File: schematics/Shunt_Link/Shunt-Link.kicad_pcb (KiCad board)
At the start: 2 copper layers, 20.3 x 8.4 mm, 17 parts, among them IC1 AD8221TRMZ-EP, IC2 AD8221TRMZ-EP, IC3 AD8244ARMZ, J1 PCIe_1x_Bus, J2 Conn_01x05_Socket

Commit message: Updated to git
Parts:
- removed IC3: AD8244ARMZ, APT_Needs:AD8244ARMZ
- added L1: AD8244ARMZ, Link_Footprints:AD8244ARMZ, F.Cu at (98.7, 79.2)
- D1: value LED_Lights -> WP130WCP_2EGW; footprint APT_Needs:LED_Lights -> Link_Footprints:LED_Lights
- IC1, IC2: footprint APT_Needs:AD8221TRMZ-EP -> Link_Footprints:AD8221TRMZ-EP
- J1: value PCIe_1x_Bus -> PCIE-036-02-X-D-TH; footprint Connector_PCBEdge:BUS_PCIexpress_x1 -> Link_Footprints:SAMTEC_PCIE_1x
- J2: footprint APT_Needs:Phoenix_Contact_MSTBA-LR -> Link_Footprints:Phoenix_Contact_MSTBA,5-LR
- TP1, TP2, TP3: value Keystone_1045 -> 1045; footprint APT_Needs:Keystone_1045 -> Link_Footprints:Keystone_1045
- moved R5 60.3 mm to (92.8, 61.8)
- moved R6 60.3 mm to (92.8, 64.8)
- moved D1 46.7 mm to (100.0, 68.9)
- moved R1 41.2 mm to (92.8, 50.0)
- moved R2 41.2 mm to (92.8, 53.0)
- moved R3 41.2 mm to (92.8, 55.9)
- moved R4 41.2 mm to (92.8, 58.9)
- moved Rg_1 36.8 mm to (92.8, 67.7)
- moved Rg_2 36.8 mm to (92.8, 70.7)
- moved J1 33.9 mm to (117.5, 80.9)
- moved TP1 33.3 mm to (115.2, 65.6)
- moved TP2 33.3 mm to (115.2, 69.7)
- moved TP3 33.3 mm to (115.2, 73.8)
- moved J2 29.3 mm to (104.8, 52.1), turned to 0 degrees
- moved IC2 16.5 mm to (125.8, 70.7)
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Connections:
- J1 pad A1: unconnected-(J1-PadA1) -> /NC
- J1 pad A10: unconnected-(J1-PadA10) -> /NC
- J1 pad A11: unconnected-(J1-PadA11) -> /NC
- J1 pad A12: unconnected-(J1-PadA12) -> /NC
- J1 pad A13: unconnected-(J1-PadA13) -> /NC
- J1 pad A14: unconnected-(J1-PadA14) -> /NC
- J1 pad A15: unconnected-(J1-PadA15) -> /NC
- J1 pad A16: unconnected-(J1-PadA16) -> /NC
- J1 pad A17: unconnected-(J1-PadA17) -> /NC
- J1 pad A18: unconnected-(J1-PadA18) -> /NC
- J1 pad A2: unconnected-(J1-PadA2) -> /NC
- J1 pad A3: unconnected-(J1-PadA3) -> /NC
- J1 pad A4: unconnected-(J1-PadA4) -> /NC
- J1 pad A5: unconnected-(J1-PadA5) -> /NC
- J1 pad A6: unconnected-(J1-PadA6) -> /NC
- J1 pad A7: unconnected-(J1-PadA7) -> /NC
- J1 pad A8: unconnected-(J1-PadA8) -> /NC
- J1 pad A9: unconnected-(J1-PadA9) -> /NC
- J1 pad B14: unconnected-(J1-PadB14) -> /NC
- J1 pad B15: unconnected-(J1-PadB15) -> /NC
- J1 pad B16: unconnected-(J1-PadB16) -> /NC
- J1 pad B3: unconnected-(J1-PadB3) -> /NC
- J1 pad B4: unconnected-(J1-PadB4) -> /NC
- J1 pad B5: unconnected-(J1-PadB5) -> /NC
- J1 pad B6: unconnected-(J1-PadB6) -> /NC
- J1 pad B7: unconnected-(J1-PadB7) -> /NC
- J1 pad B8: unconnected-(J1-PadB8) -> /NC
- J1 pad B9: unconnected-(J1-PadB9) -> /NC
- TP1 pad TP1: /S_{o} -> /S_{test}
- TP2 pad TP1: /T_{o} -> /T_{test}
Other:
- board outline removed

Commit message: Modifications to Shunt Link
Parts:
- removed D1: WP130WCP_2EGW, Link_Footprints:LED_Lights
- removed Rg_1, Rg_2: 499, Resistor_SMD:R_0805_2012Metric
- added C1: 0.1 uF, Capacitor_SMD:C_1210_3225Metric, F.Cu at (138.8, 56.5)
- added C2: 10 uF, Capacitor_SMD:C_1210_3225Metric, F.Cu at (146.5, 56.5)
- added IC3: AD8221TRMZ-EP, Link_Footprints:AD8221TRMZ-EP, F.Cu at (135.5, 99.7)
- added IC4: AD8221TRMZ-EP, Link_Footprints:AD8221TRMZ-EP, F.Cu at (135.2, 110.0)
- added J3: Conn_02x03_Odd_Even, Link_Footprints:1818517, F.Cu at (90.8, 100.5)
- added R10: R, Resistor_SMD:R_2512_6332Metric, F.Cu at (111.8, 109.8)
- added R11: R, Resistor_SMD:R_2512_6332Metric, F.Cu at (117.2, 116.0)
- added R12: R, Resistor_SMD:R_2512_6332Metric, F.Cu at (121.2, 109.9)
- added R7: R_{g3}, Resistor_SMD:R_2512_6332Metric, F.Cu at (127.8, 99.7)
- added R8: R_{shunt}, Resistor_SMD:R_2512_6332Metric, F.Cu at (122.0, 99.7)
- added R9: R_{g4}, Resistor_SMD:R_2512_6332Metric, F.Cu at (127.5, 110.0)
- added TP4: T2, Link_Footprints:KEYSTONE_5017, F.Cu at (111.5, 39.8)
- added TP5: GND, Link_Footprints:KEYSTONE_5017, F.Cu at (90.2, 50.2)
- J1: footprint Link_Footprints:SAMTEC_PCIE_1x -> Connector_PCBEdge:BUS_PCIexpress_x1
- J2: value Conn_01x05_Socket -> Conn_02x03_Odd_Even; footprint Link_Footprints:Phoenix_Contact_MSTBA,5-LR -> Link_Footprints:1818517
- R1: value 6.25 -> R_{g1}; footprint Resistor_SMD:R_0805_2012Metric -> Resistor_SMD:R_2512_6332Metric
- R2: value 6.25 -> R_{shunt}; footprint Resistor_SMD:R_0805_2012Metric -> Resistor_SMD:R_2512_6332Metric
- R3: value 10.4 -> R_{g2}; footprint Resistor_SMD:R_0805_2012Metric -> Resistor_SMD:R_2512_6332Metric
- R4, R5: value 50 -> R; footprint Resistor_SMD:R_0805_2012Metric -> Resistor_SMD:R_2512_6332Metric
- R6: value 20.8 -> R; footprint Resistor_SMD:R_0805_2012Metric -> Resistor_SMD:R_2512_6332Metric
- TP1: value 1045 -> S1; footprint Link_Footprints:Keystone_1045 -> Link_Footprints:KEYSTONE_5017
- TP2: value 1045 -> T1; footprint Link_Footprints:Keystone_1045 -> Link_Footprints:KEYSTONE_5017
- TP3: value 1045 -> S2; footprint Link_Footprints:Keystone_1045 -> Link_Footprints:KEYSTONE_5017
- moved J1 50.4 mm to (136.0, 127.8)
- moved L1 43.1 mm to (102.0, 36.2)
- moved TP3 42.5 mm to (90.2, 39.4)
- moved R3 41.4 mm to (128.0, 77.7), turned to -90 degrees
- moved TP1 41.3 mm to (90.2, 32.8)
- moved TP2 37.1 mm to (111.5, 32.8)
- moved R1 35.9 mm to (124.8, 66.2), turned to -90 degrees
- moved R5 33.9 mm to (118.2, 84.2), turned to 180 degrees
- moved R6 31.3 mm to (121.2, 77.7), turned to -90 degrees
- moved R4 28.7 mm to (114.5, 77.6), turned to -90 degrees
- moved R2 27.6 mm to (117.0, 66.2), turned to -90 degrees
- moved J2 20.3 mm to (91.0, 67.0), turned to -90 degrees
- moved IC2 11.8 mm to (135.2, 77.8)
- moved IC1 9.24 mm to (135.0, 66.0)
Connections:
- IC1 pad 1: /S_{+} -> /S_{1+}
- IC1 pad 4: /GND -> GND
- IC1 pad 5: /GND -> GND
- IC1 pad 6: /V_{ref} -> /+2V5
- IC1 pad 7: /S_{o} -> /S_{1out}
- IC1 pad 8: /V_{s} -> +12V
- IC2 pad 1: /T_{+} -> /T_{1-}
- IC2 pad 4: /GND -> Net-(IC2-+IN)
- IC2 pad 5: /GND -> GND
- IC2 pad 7: /T_{o} -> /T_{1out}
- IC2 pad 8: /V_{s} -> unconnected-(IC2-+VS-Pad8)
- J1 pad A1: /NC -> unconnected-(J1-PadA1)
- J1 pad A10: /NC -> unconnected-(J1-PadA10)
- J1 pad A11: /NC -> unconnected-(J1-PadA11)
- J1 pad A12: /NC -> unconnected-(J1-PadA12)
- J1 pad A13: /NC -> unconnected-(J1-PadA13)
- J1 pad A14: /NC -> unconnected-(J1-PadA14)
- J1 pad A15: /NC -> unconnected-(J1-PadA15)
- J1 pad A16: /NC -> unconnected-(J1-PadA16)
- J1 pad A17: /NC -> unconnected-(J1-PadA17)
- J1 pad A18: /NC -> unconnected-(J1-PadA18)
- J1 pad A2: /NC -> unconnected-(J1-PadA2)
- J1 pad A3: /NC -> unconnected-(J1-PadA3)
- J1 pad A4: /NC -> unconnected-(J1-PadA4)
- J1 pad A5: /NC -> unconnected-(J1-PadA5)
- J1 pad A6: /NC -> unconnected-(J1-PadA6)
- J1 pad A7: /NC -> unconnected-(J1-PadA7)
- J1 pad A8: /NC -> unconnected-(J1-PadA8)
- J1 pad A9: /NC -> unconnected-(J1-PadA9)
- J1 pad B1: /S_{o} -> /S_{2out}
- J1 pad B10: /Green_{1} -> unconnected-(J1-PadB10)
- J1 pad B11: /Red_{1} -> unconnected-(J1-PadB11)
- J1 pad B12: /Green_{2} -> unconnected-(J1-PadB12)
- J1 pad B13: /Red_{2} -> unconnected-(J1-PadB13)
- J1 pad B14: /NC -> unconnected-(J1-PadB14)
- J1 pad B15: /NC -> unconnected-(J1-PadB15)
- J1 pad B16: /NC -> unconnected-(J1-PadB16)
- J1 pad B17: /V_{s} -> +12V
- J1 pad B18: /GND -> GND
- J1 pad B2: /T_{o} -> /T_{2out}
- J1 pad B3: /NC -> /T_{1out}
- J1 pad B4: /NC -> /S_{1out}
- J1 pad B5: /NC -> unconnected-(J1-PadB5)
- J1 pad B6: /NC -> unconnected-(J1-PadB6)
- J1 pad B7: /NC -> unconnected-(J1-PadB7)
- J1 pad B8: /NC -> unconnected-(J1-PadB8)
- J1 pad B9: /NC -> unconnected-(J1-PadB9)
- J2 pad 1: /GND -> +12V
- J2 pad 2: /V_{+} -> /S_{1+}
- J2 pad 3: /T_{+} -> /T_{1-}
- J2 pad 4: /V_{+} -> +12V
- J2 pad 5: /S_{+} -> unconnected-(J2-Pin_5-Pad5)
- L1 pad 1: /V_{2.5} -> /S_{1out}
- L1 pad 10: /T_{o} -> /T_{1test}
- L1 pad 2: /V_{ref} -> /S_{1test}
- L1 pad 3: /V_{s} -> +12V
- L1 pad 4: /V_{+} -> /S_{2test}
- L1 pad 5: /V_{5} -> /S_{2out}
- L1 pad 6: /S_{o} -> /T_{2test}
- L1 pad 7: /S_{test} -> /T_{2out}
- L1 pad 8: /GND -> GND
- L1 pad 9: /T_{test} -> /T_{1out}
- R1 pad 1: /S_{+} -> Net-(IC1-RG_1)
- R1 pad 2: /GND -> Net-(IC1-RG_2)
- R2 pad 1: /T_{+} -> /S_{1+}
- R2 pad 2: /GND -> GND
- R3 pad 1: /V_{2.5} -> Net-(IC2-RG_1)
- R3 pad 2: /GND -> Net-(IC2-RG_2)
- R4 pad 1: /V_{s} -> /T_{1-}
- R4 pad 2: /V_{2.5} -> GND
- R5 pad 1: /V_{s} -> Net-(IC2-+IN)
- R5 pad 2: /V_{5} -> GND
- R6 pad 1: /V_{5} -> +12V
- R6 pad 2: /GND -> Net-(IC2-+IN)
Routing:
- net /S_{1out}: track 0.00 -> 119.9 mm
- net /T_{1out}: track 0.00 -> 114.8 mm, vias 0 -> 2
- net /S_{2out}: track 0.00 -> 112.4 mm
- net /T_{2out}: track 0.00 -> 110.6 mm, vias 0 -> 2
- net GND: track 0.00 -> 65.4 mm, vias 0 -> 13
- net /S_{2+}: track 0.00 -> 47.4 mm
- net /S_{1+}: track 0.00 -> 46.5 mm
- net /T_{1-}: track 0.00 -> 45.0 mm
- net /T_{2-}: track 0.00 -> 44.6 mm
- net Net-(IC2-+IN): track 0.00 -> 17.7 mm
- net Net-(IC4-+IN): track 0.00 -> 17.5 mm
- net /S_{1test}: track 0.00 -> 10.7 mm
- net /S_{2test}: track 0.00 -> 10.6 mm
- net Net-(IC1-RG_2): track 0.00 -> 9.22 mm
- net Net-(IC1-RG_1): track 0.00 -> 9.14 mm
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- added copper zone on F.Cu, net +12V
- added copper zone on B.Cu, net GND
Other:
- board outline added: 78.2 x 96 mm
- board text added: "OATS Center Shunt-Link v1 (10/13/2025) abalmos@purdue.edu"

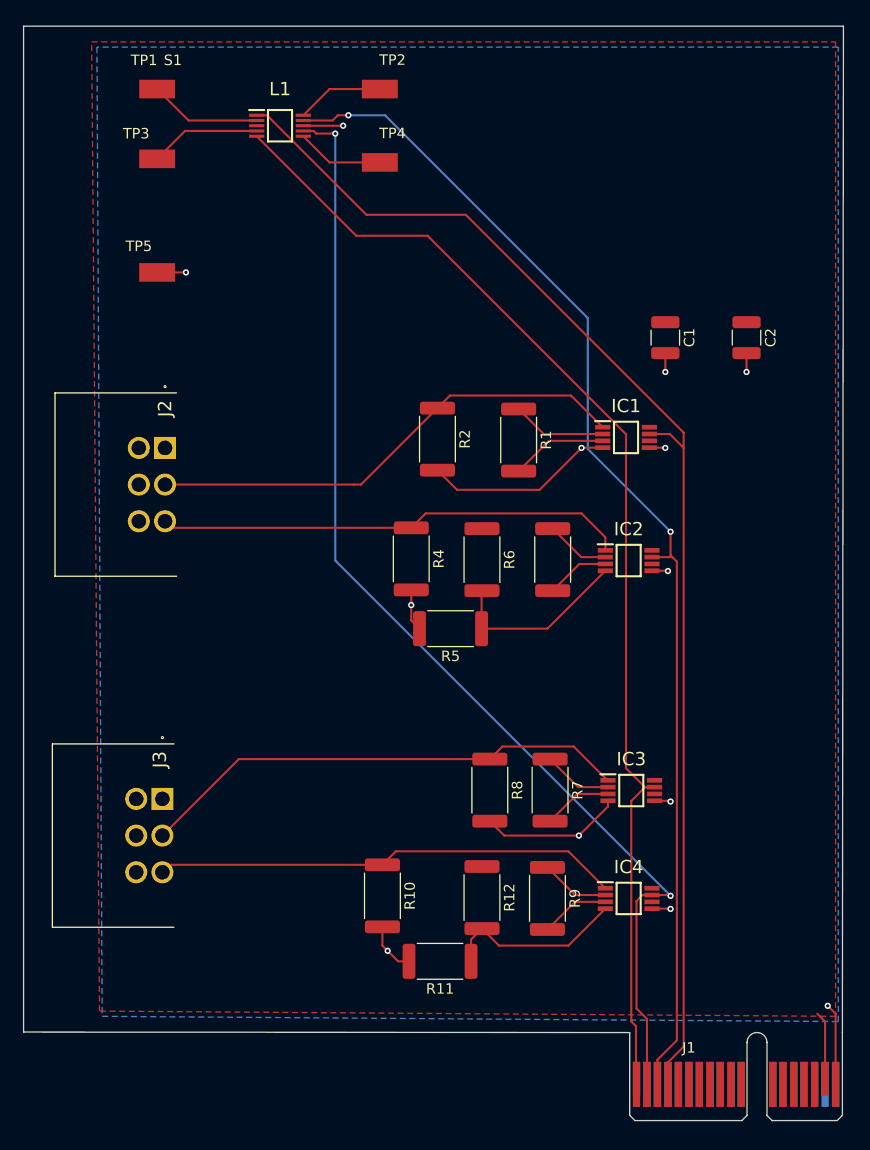
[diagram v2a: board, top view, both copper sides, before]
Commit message: Start rev2
- Smaller resistors
- Swap filled zones (GND should be top layer)
- Extend filled zones to edges
- Give each in-amp capacitors
- Fix IC trace angles (Should only come out at 90 degrees)
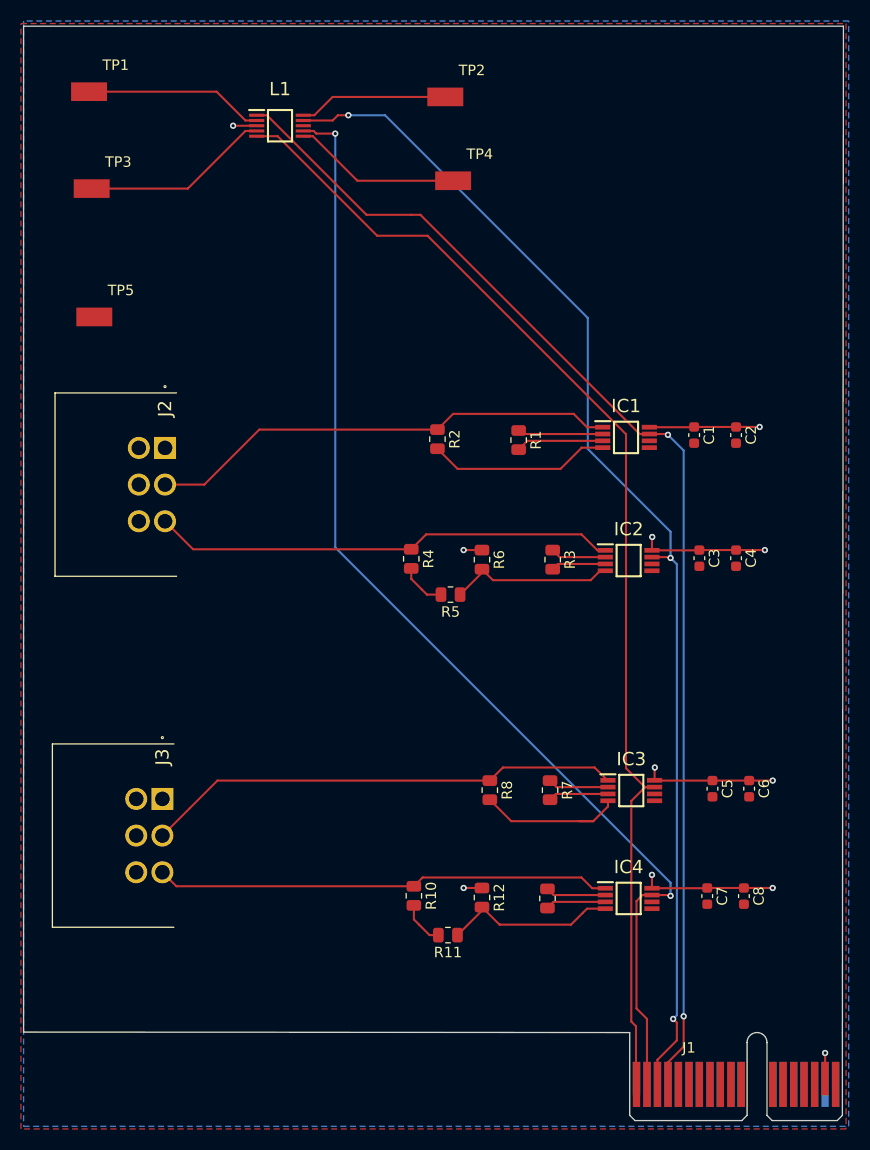
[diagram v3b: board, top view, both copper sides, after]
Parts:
- added C3: 0.1 uF, Capacitor_SMD:C_0603_1608Metric, F.Cu at (142.0, 77.5)
- added C4: 10 uF, Capacitor_SMD:C_0603_1608Metric, F.Cu at (145.5, 77.5)
- added C5: 0.1 uF, Capacitor_SMD:C_0603_1608Metric, F.Cu at (143.2, 99.5)
- added C6: 10 uF, Capacitor_SMD:C_0603_1608Metric, F.Cu at (146.8, 99.5)
- added C7: 0.1 uF, Capacitor_SMD:C_0603_1608Metric, F.Cu at (142.8, 109.8)
- added C8: 10 uF, Capacitor_SMD:C_0603_1608Metric, F.Cu at (146.2, 109.8)
- C1, C2: footprint Capacitor_SMD:C_1210_3225Metric -> Capacitor_SMD:C_0603_1608Metric
- R1, R10, R11, R12, R2, R3, R4, R5, R6, R7, R8, R9: footprint Resistor_SMD:R_2512_6332Metric -> Resistor_SMD:R_0805_2012Metric
- moved C1 9.70 mm to (141.5, 65.8)
- moved C2 9.35 mm to (145.5, 65.8)
- moved TP5 7.35 mm to (84.2, 54.5)
- moved TP4 7.22 mm to (118.5, 41.5)
- moved TP3 6.86 mm to (84.0, 42.2)
- moved TP1 6.50 mm to (83.8, 33.0)
- moved TP2 6.29 mm to (117.8, 33.5)
- moved R5 3.25 mm to (118.2, 81.0)
- moved R10 3.00 mm to (114.8, 109.8)
- moved R11 2.61 mm to (118.0, 113.5)
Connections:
- IC2 pad 8: unconnected-(IC2-+VS-Pad8) -> +12V
- IC3 pad 8: unconnected-(IC3-+VS-Pad8) -> +12V
- IC4 pad 8: unconnected-(IC4-+VS-Pad8) -> +12V
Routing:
- net +12V: track 6.76 -> 56.7 mm, vias 0 -> 11
- net GND: track 65.4 -> 40.8 mm, vias 13 -> 0
- net /T_{2test}: track 8.34 -> 16.1 mm
- net /S_{2test}: track 10.6 -> 18.0 mm
- net /S_{1test}: track 10.7 -> 17.1 mm
- net /T_{1test}: track 8.34 -> 14.3 mm
- net /S_{1out}: track 119.9 -> 115.1 mm, vias 0 -> 2
- net Net-(IC2-+IN): track 17.7 -> 15.9 mm
- net /S_{2+}: track 47.4 -> 45.7 mm
- net /S_{1+}: track 46.5 -> 45.1 mm
- net Net-(IC4-RG_2): track 6.62 -> 5.77 mm
- net Net-(IC4-RG_1): track 6.62 -> 5.77 mm
- net Net-(IC1-RG_2): track 9.22 -> 8.37 mm
- net Net-(IC3-RG_2): track 6.60 -> 5.75 mm
- net Net-(IC2-RG_1): track 6.15 -> 5.30 mm
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- added copper zone on B.Cu, net +12V
- added copper zone on F.Cu, net GND
- removed copper zone on F.Cu, net +12V
- removed copper zone on B.Cu, net GND
